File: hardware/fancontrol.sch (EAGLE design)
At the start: 11 parts, among them Q1 IRLZ44Z, T1 BC547

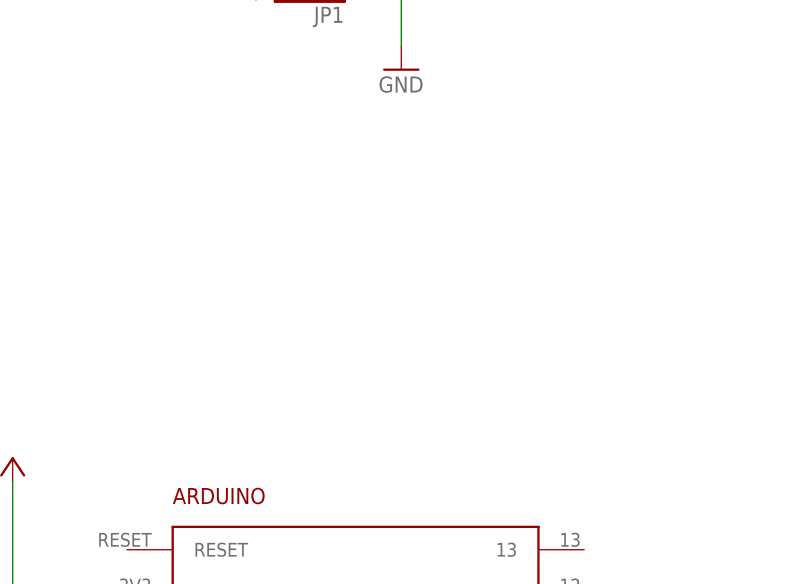
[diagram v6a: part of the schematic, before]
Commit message: added capacitors to Vin. Fixes #1
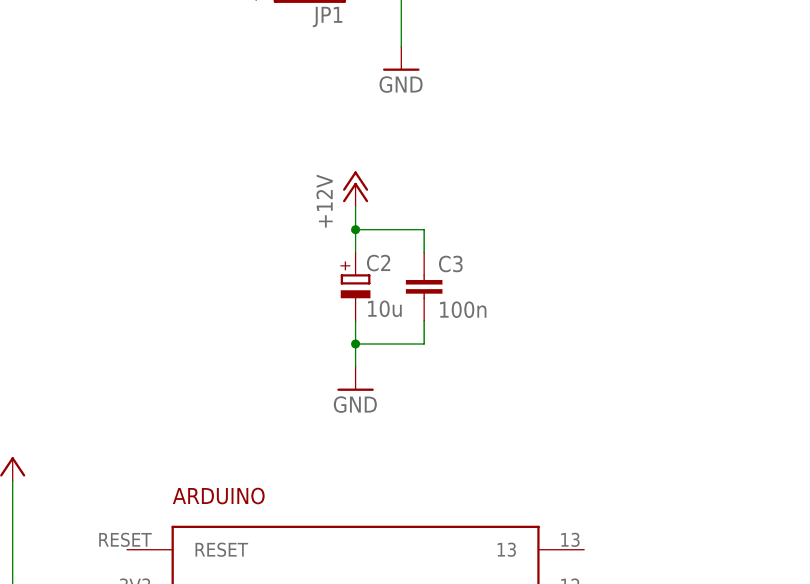
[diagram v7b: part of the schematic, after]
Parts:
- added C2: 10u, rcl:CPOL-EUE2.5-5
- added C3: 100n, rcl:C-EU025-025X050
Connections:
- net +12V: now also C2.+, C3.1
- net GND: now also C2.-, C3.2
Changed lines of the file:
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@@
 <part name="R5" library="rcl" deviceset="R-EU_" device="0207/7" value="10k"/>
 <part name="P+5" library="supply1" deviceset="+5V" device=""/>
+<part name="C2" library="rcl" deviceset="CPOL-EU" device="E2.5-5" value="10u"/>
+<part name="C3" library="rcl" deviceset="C-EU" device="025-025X050" value="100n"/>
+<part name="GND6" library="supply1" deviceset="GND" device=""/>
+<part name="P+6" library="supply1" deviceset="+12V" device=""/>
 </parts>
 <sheets>
@@
 <instance part="R5" gate="G$1" x="200.66" y="119.38" rot="R90"/>
 <instance part="P+5" gate="1" x="200.66" y="129.54"/>
+<instance part="C2" gate="G$1" x="50.8" y="111.76"/>
+<instance part="C3" gate="G$1" x="58.42" y="111.76"/>
+<instance part="GND6" gate="1" x="50.8" y="99.06"/>
+<instance part="P+6" gate="1" x="50.8" y="121.92"/>
 </instances>
 <busses>
@@
 <wire x1="200.66" y1="109.22" x2="200.66" y2="104.14" width="0.1524" layer="91"/>
 </segment>
+<segment>
+<pinref part="C2" gate="G$1" pin="-"/>
+<pinref part="GND6" gate="1" pin="GND"/>
+<wire x1="50.8" y1="106.68" x2="50.8" y2="104.14" width="0.1524" layer="91"/>
+<pinref part="C3" gate="G$1" pin="2"/>
+<wire x1="50.8" y1="104.14" x2="50.8" y2="101.6" width="0.1524" layer="91"/>
+<wire x1="58.42" y1="106.68" x2="58.42" y2="104.14" width="0.1524" layer="91"/>
+<wire x1="58.42" y1="104.14" x2="50.8" y2="104.14" width="0.1524" layer="91"/>
+<junction x="50.8" y="104.14"/>
+</segment>
 </net>
 <net name="N$3" class="0">
@@
 <wire x1="5.08" y1="60.96" x2="5.08" y2="88.9" width="0.1524" layer="91"/>
 </segment>
+<segment>
+<pinref part="C2" gate="G$1" pin="+"/>
+<wire x1="50.8" y1="119.38" x2="50.8" y2="116.84" width="0.1524" layer="91"/>
+<pinref part="C3" gate="G$1" pin="1"/>
+<wire x1="50.8" y1="116.84" x2="50.8" y2="114.3" width="0.1524" layer="91"/>
+<wire x1="58.42" y1="114.3" x2="58.42" y2="116.84" width="0.1524" layer="91"/>
+<wire x1="58.42" y1="116.84" x2="50.8" y2="116.84" width="0.1524" layer="91"/>
+<junction x="50.8" y="116.84"/>
+<pinref part="P+6" gate="1" pin="+12V"/>
+</segment>
 </net>

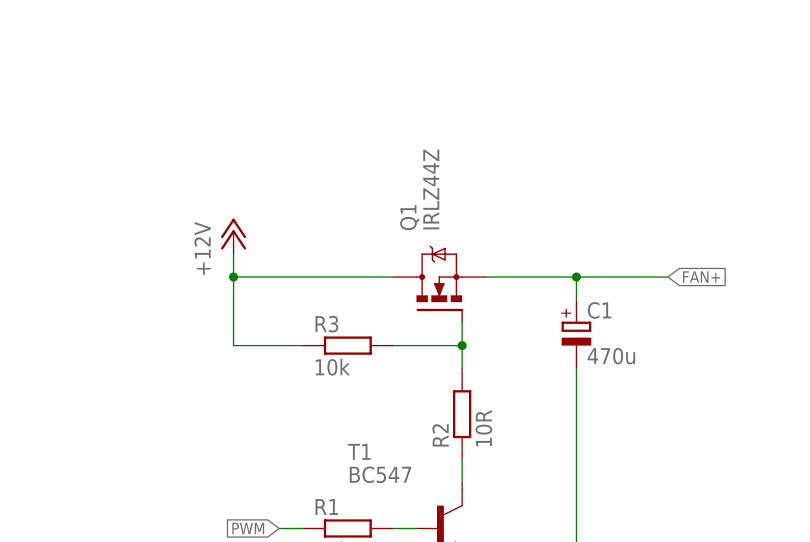
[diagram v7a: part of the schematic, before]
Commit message: Replace transistor, make routes wider
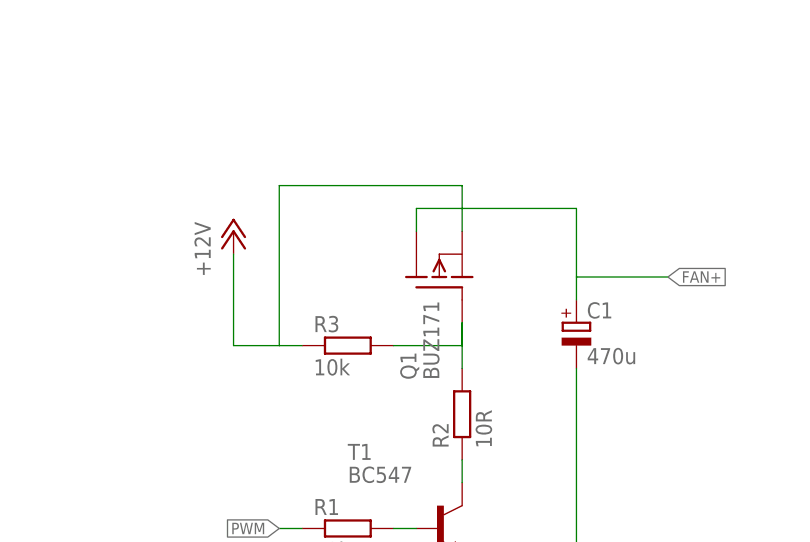
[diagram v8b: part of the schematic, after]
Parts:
- Q1: value IRLZ44Z -> BUZ171; device transistor-power:IRLZ44Z -> transistor-fet:BUZ171
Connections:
- net +12V: now also Q1.S; no longer Q1.D
- net FAN+: now also Q1.D; no longer Q1.S
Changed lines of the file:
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@@
 <?xml version="1.0" encoding="utf-8"?>
 <!DOCTYPE eagle SYSTEM "eagle.dtd">
-<eagle version="6.4">
+<eagle version="6.3">
 <drawing>
 <settings>
@@
 <part name="P+2" library="supply1" deviceset="+12V" device=""/>
 <part name="GND1" library="supply1" deviceset="GND" device=""/>
-<part name="Q1" library="transistor-power" deviceset="IRLZ44Z" device=""/>
+<part name="Q1" library="transistor-fet" deviceset="BUZ171" device=""/>
 <part name="R1" library="rcl" deviceset="R-EU_" device="0207/7" value="10k"/>
 <part name="T1" library="transistor" deviceset="BC547" device=""/>
@@
 <instance part="P+2" gate="1" x="111.76" y="137.16"/>
 <instance part="GND1" gate="1" x="137.16" y="93.98"/>
-<instance part="Q1" gate="G$1" x="134.62" y="129.54" rot="R90"/>
+<instance part="Q1" gate="G$1" x="134.62" y="132.08" rot="R90"/>
 <instance part="R1" gate="G$1" x="124.46" y="104.14"/>
 <instance part="T1" gate="G$1" x="134.62" y="104.14"/>
@@
 </segment>
 </net>
-<net name="N$3" class="0">
-<segment>
-<pinref part="R2" gate="G$1" pin="2"/>
-<pinref part="Q1" gate="G$1" pin="G"/>
-<wire x1="137.16" y1="121.92" x2="137.16" y2="124.46" width="0.1524" layer="91"/>
-<pinref part="R3" gate="G$1" pin="2"/>
-<wire x1="137.16" y1="124.46" x2="137.16" y2="127" width="0.1524" layer="91"/>
-<wire x1="129.54" y1="124.46" x2="137.16" y2="124.46" width="0.1524" layer="91"/>
-<junction x="137.16" y="124.46"/>
-</segment>
-</net>
 <net name="+12V" class="0">
 <segment>
-<pinref part="Q1" gate="G$1" pin="D"/>
 <pinref part="P+2" gate="1" pin="+12V"/>
-<wire x1="129.54" y1="132.08" x2="111.76" y2="132.08" width="0.1524" layer="91"/>
-<wire x1="111.76" y1="132.08" x2="111.76" y2="134.62" width="0.1524" layer="91"/>
 <pinref part="R3" gate="G$1" pin="1"/>
-<wire x1="119.38" y1="124.46" x2="111.76" y2="124.46" width="0.1524" layer="91"/>
-<wire x1="111.76" y1="124.46" x2="111.76" y2="132.08" width="0.1524" layer="91"/>
-<junction x="111.76" y="132.08"/>
+<wire x1="119.38" y1="124.46" x2="116.84" y2="124.46" width="0.1524" layer="91"/>
+<wire x1="116.84" y1="124.46" x2="111.76" y2="124.46" width="0.1524" layer="91"/>
+<wire x1="111.76" y1="124.46" x2="111.76" y2="134.62" width="0.1524" layer="91"/>
+<pinref part="Q1" gate="G$1" pin="S"/>
+<wire x1="137.16" y1="137.16" x2="137.16" y2="142.24" width="0.1524" layer="91"/>
+<wire x1="137.16" y1="142.24" x2="116.84" y2="142.24" width="0.1524" layer="91"/>
+<wire x1="116.84" y1="142.24" x2="116.84" y2="124.46" width="0.1524" layer="91"/>
 </segment>
 <segment>
@@
 <net name="FAN+" class="0">
 <segment>
-<pinref part="Q1" gate="G$1" pin="S"/>
 <pinref part="C1" gate="G$1" pin="+"/>
-<wire x1="139.7" y1="132.08" x2="149.86" y2="132.08" width="0.1524" layer="91"/>
 <wire x1="149.86" y1="132.08" x2="149.86" y2="129.54" width="0.1524" layer="91"/>
 <wire x1="149.86" y1="132.08" x2="160.02" y2="132.08" width="0.1524" layer="91"/>
-<junction x="149.86" y="132.08"/>
 <label x="160.02" y="132.08" size="1.27" layer="95" xref="yes"/>
+<pinref part="Q1" gate="G$1" pin="D"/>
+<wire x1="132.08" y1="137.16" x2="132.08" y2="139.7" width="0.1524" layer="91"/>
+<wire x1="132.08" y1="139.7" x2="149.86" y2="139.7" width="0.1524" layer="91"/>
+<wire x1="149.86" y1="139.7" x2="149.86" y2="132.08" width="0.1524" layer="91"/>
 </segment>
 <segment>
@@
 </segment>
 </net>
+<net name="N$3" class="0">
+<segment>
+<pinref part="R3" gate="G$1" pin="2"/>
+<pinref part="Q1" gate="G$1" pin="G"/>
+<wire x1="129.54" y1="124.46" x2="137.16" y2="124.46" width="0.1524" layer="91"/>
+<wire x1="137.16" y1="124.46" x2="137.16" y2="127" width="0.1524" layer="91"/>
+<pinref part="R2" gate="G$1" pin="2"/>
+<wire x1="137.16" y1="127" x2="137.16" y2="121.92" width="0.1524" layer="91"/>
+</segment>
+</net>
